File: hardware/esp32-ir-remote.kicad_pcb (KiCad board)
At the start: 2 copper layers, 80 x 55 mm, 76 parts, among them J2 USB_C_Receptacle_USB2.0_14P, J3 Qwiic_I2C, J4 GPIO_PWR, J5 EXT_IR, J6 JTAG, Q1 Q_NPN_BCE, Q2 Q_NPN_BCE, Q3 IRLML6344, Q4 2N7002, Q5 2N7002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

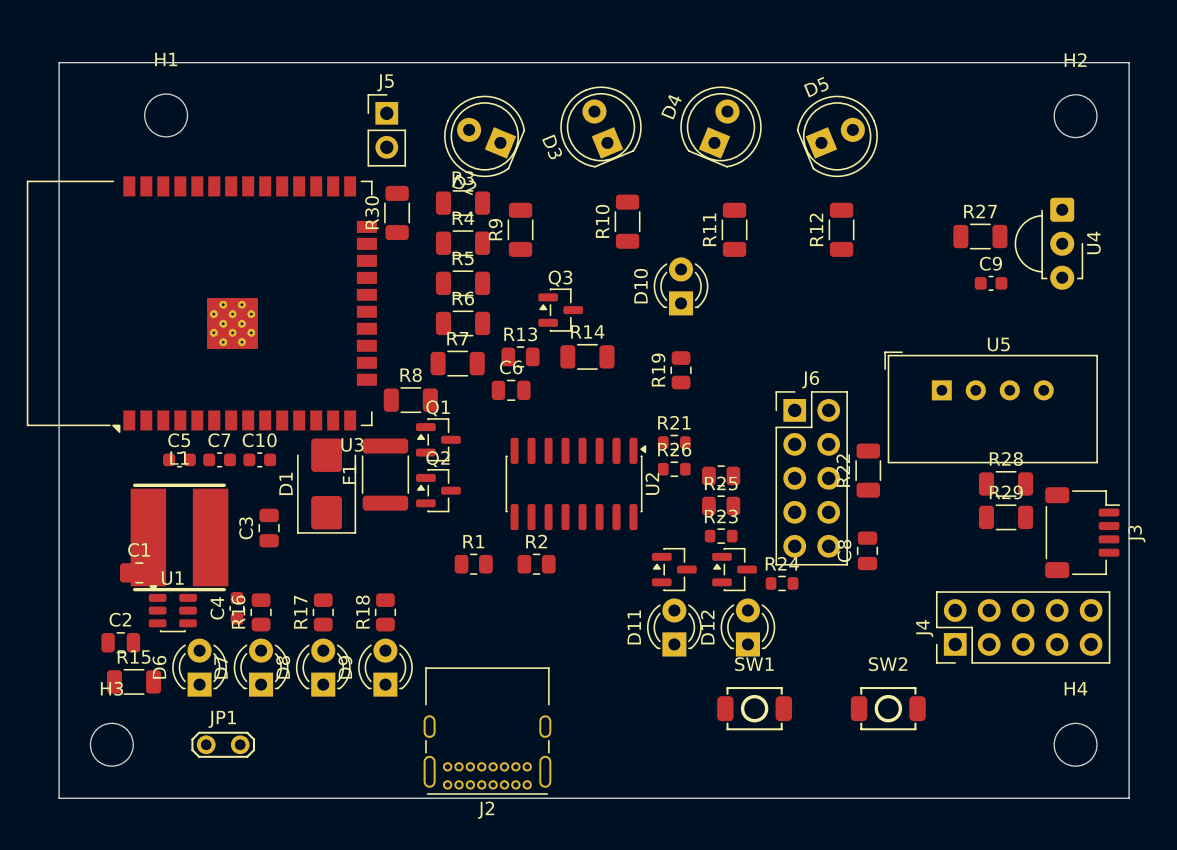
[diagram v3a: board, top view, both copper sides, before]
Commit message: H2.3 WIP: routed board v11 (1010 tracks, 143 vias, 17 legs open) + routing toolchain
- scripts/pcb_router.py: deterministic A* grid router (0.1mm grid, netclass
  widths, antenna keepout, J2 seed stubs, power-prefers-B, corridor penalties)
- scripts/pcb_finish.py: connectivity finisher with bounded rip-up + history
- scripts/pcb_pour.py: GND pours both layers + antenna keepout rule areas +
  stitching vias (not yet run)
- scripts/pcb_silk.py, scripts/drc_summary.py: silk + DRC passes (pending)
- placement deltas during routing: H1 into antenna-wedge corner (nylon screw
  note), J5/R30 west, C6 beside U2, R5-R7 pullups to NE, board min
  clearance/track relaxed to JLCPCB floor 0.127
- scripts/build-site.sh: PCB renders + GLB + interactive 3D viewer page
- hardware/bring-up.md: power-on test procedure (H3.3)
- USB-C dual-orientation D+/D- cross resolved via per-layer THT stubs
Remaining 17 unrouted legs concentrated in the EN/auto-reset cluster - being
finished by pcb_finish.py + hand-routing; DRC pass follows.
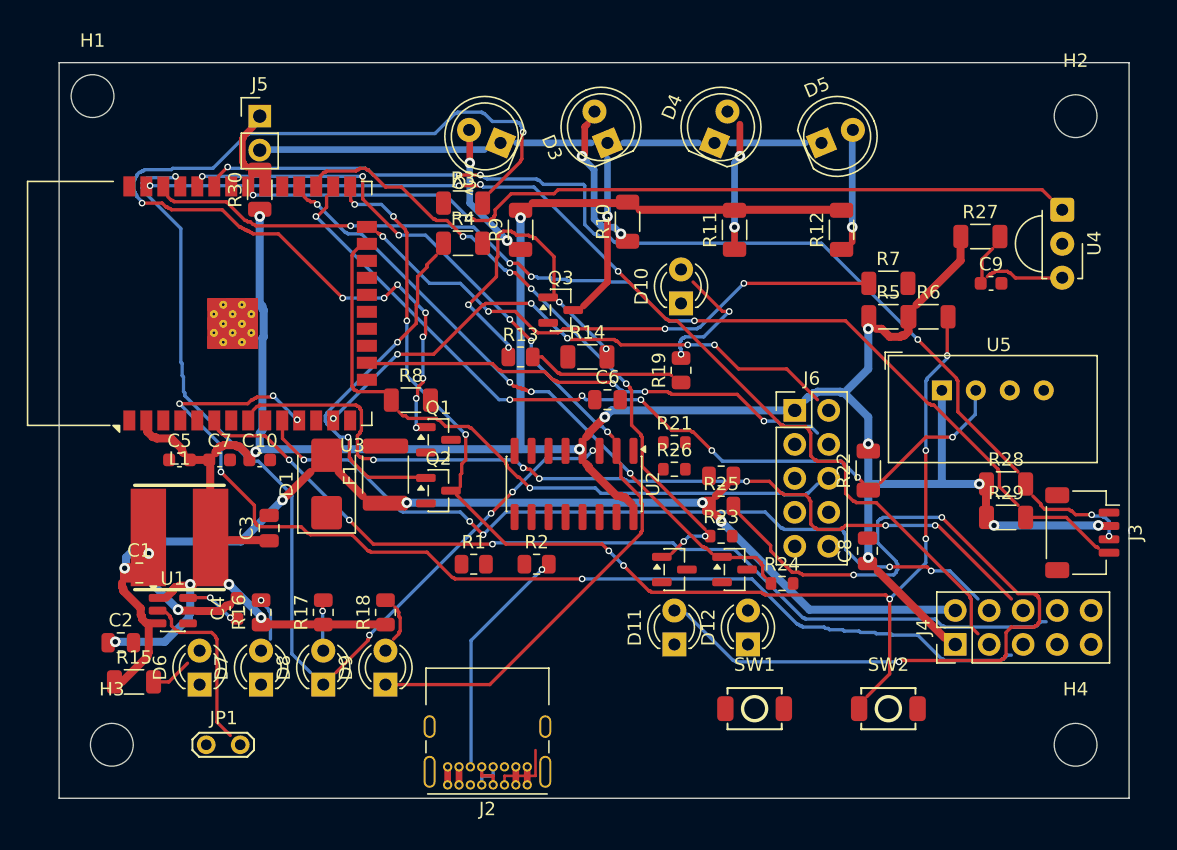
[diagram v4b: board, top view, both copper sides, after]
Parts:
- moved R6 34.8 mm to (165.0, 79.0)
- moved R7 32.8 mm to (162.0, 76.5)
- moved R5 31.9 mm to (162.0, 79.0)
- moved R30 10.4 mm to (115.0, 69.5)
- moved J5 9.50 mm to (115.0, 64.0)
- moved C6 7.23 mm to (141.0, 85.2)
- moved H1 5.69 mm to (102.5, 62.5)
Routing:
- net +3.3V: track 0.00 -> 191.0 mm, vias 0 -> 15
- net ESP_GPIO0: track 0.00 -> 92.2 mm, vias 0 -> 10
- net ESP_GPIO26: track 0.00 -> 82.0 mm, vias 0 -> 5
- net ESP_GPIO21: track 0.00 -> 80.3 mm, vias 0 -> 6
- net ESP_GPIO22: track 0.00 -> 79.7 mm, vias 0 -> 4
- net ESP_GPIO23: track 0.00 -> 79.4 mm, vias 0 -> 4
- net Net-(Q1-B): track 0.00 -> 74.0 mm, vias 0 -> 10
- net +5V: track 0.00 -> 72.0 mm, vias 0 -> 5
- net UART_TX: track 0.00 -> 71.4 mm, vias 0 -> 5
- net UART_RX: track 0.00 -> 69.3 mm, vias 0 -> 6
- net ESP_GPIO34: track 0.00 -> 68.2 mm, vias 0 -> 3
- net ESP_GPIO32: track 0.00 -> 66.6 mm, vias 0 -> 6
- net Net-(D11-A): track 0.00 -> 65.1 mm, vias 0 -> 3
- net IR_RX: track 0.00 -> 61.9 mm, vias 0 -> 2
- net TEMP_DATA: track 0.00 -> 61.6 mm, vias 0 -> 7
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
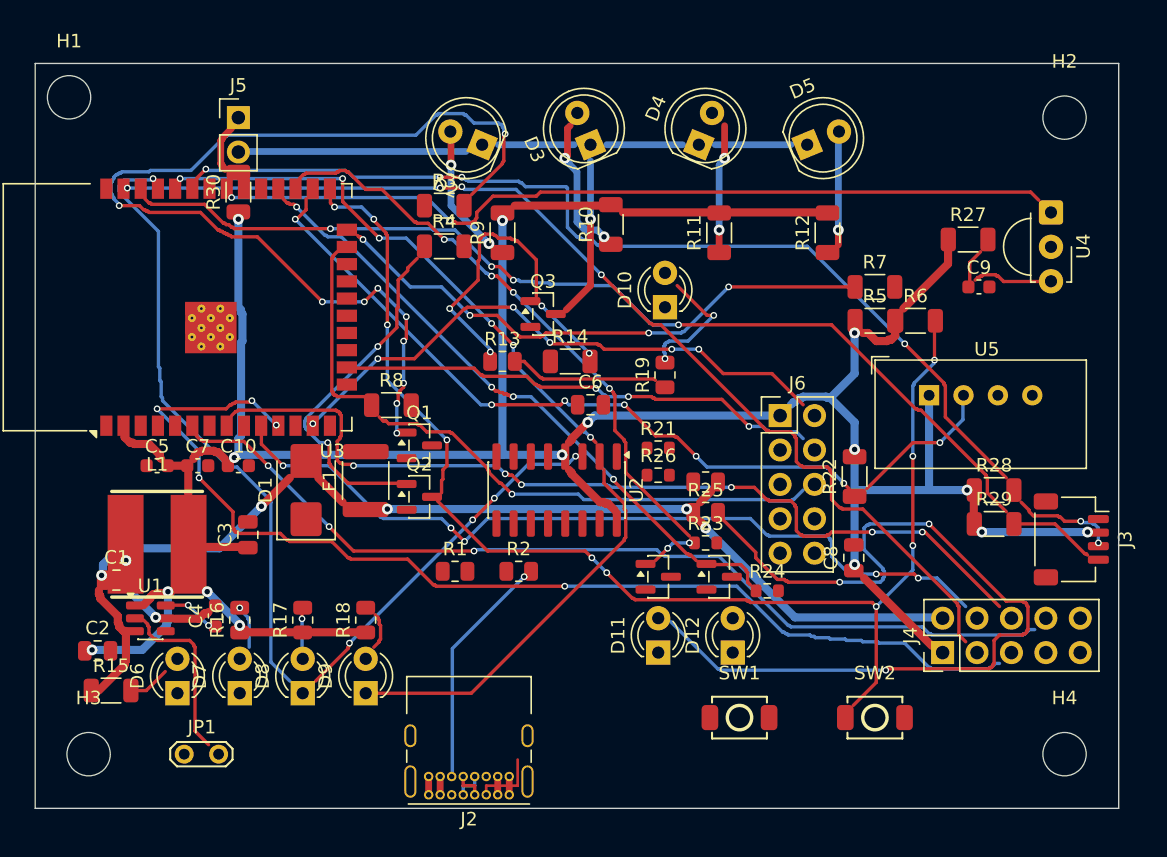
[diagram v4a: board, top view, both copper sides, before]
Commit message: H2.3: routing COMPLETE - all nets connected
Final sequence: local-families-first ordering, transit highways rerouted
around the module pad row, R5/R6/R7 pullup pitch fix (the entire ESP_EN
failure traced to R5/R6 courtyard overlap entombing R5's pad), R23
relocated to free space, connectivity finisher converged round 2:
ALL NETS CONNECTED (machine-verified component analysis of pads+tracks+vias).
Courtyards: 1 accepted exception (H1 in the antenna-wedge corner, nylon
screw documented in bring-up.md).
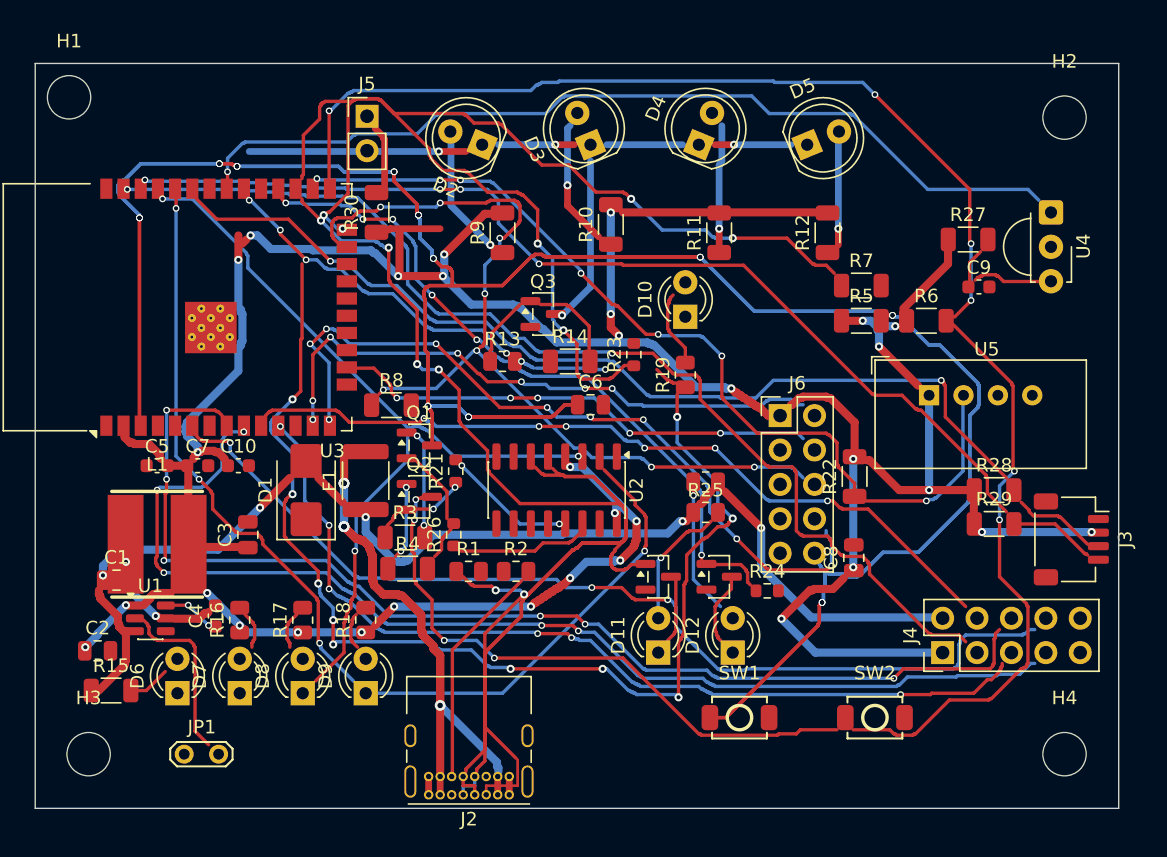
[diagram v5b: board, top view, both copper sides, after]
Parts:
- moved R3 24.7 mm to (127.3, 95.0)
- moved R4 24.0 mm to (127.5, 97.3)
- moved R26 15.7 mm to (130.9, 94.8), turned to 90 degrees
- moved R21 15.0 mm to (131.1, 90.1), turned to 90 degrees
- moved R23 14.9 mm to (144.2, 81.5), turned to 90 degrees
- moved R30 10.3 mm to (125.2, 71.0)
- moved J5 9.50 mm to (124.5, 63.9)
- moved D10 1.66 mm to (148.0, 78.7)
- moved R19 1.50 mm to (148.0, 83.0)
- moved R7 1.00 mm to (161.0, 76.4)
- moved R1 1.00 mm to (132.0, 97.5)
- moved R5 1.00 mm to (161.0, 79.0)
- moved R6 0.80 mm to (165.8, 79.0)
- moved R2 0.20 mm to (135.5, 97.5)
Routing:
- net ESP_EN: track 0.00 -> 311.4 mm, vias 0 -> 22
- net IR_TX: track 10.5 -> 117.0 mm, vias 0 -> 16
- net ESP_GPIO33: track 0.00 -> 84.3 mm, vias 0 -> 5
- net Net-(Q1-B): track 74.0 -> 6.81 mm, vias 10 -> 2
- net ESP_GPIO0: track 92.2 -> 154.2 mm
- net Net-(D11-A): track 65.1 -> 8.50 mm, vias 3 -> 1
- net ESP_GPIO12: track 0.00 -> 56.5 mm, vias 0 -> 9
- net Net-(F1-Pad2): track 2.70 -> 58.6 mm, vias 0 -> 5
- net USER_LED1: track 46.2 -> 90.0 mm
- net +3.3V: track 191.0 -> 230.8 mm, vias 15 -> 32
- net USB_D-: track 2.20 -> 36.0 mm
- net USB_D+: track 2.20 -> 34.9 mm
- net Net-(Q2-B): track 25.3 -> 5.43 mm
- net Net-(J2-CC1): track 4.92 -> 24.2 mm, vias 0 -> 2
- net ESP_GPIO15: track 47.4 -> 65.2 mm, vias 1 -> 8
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
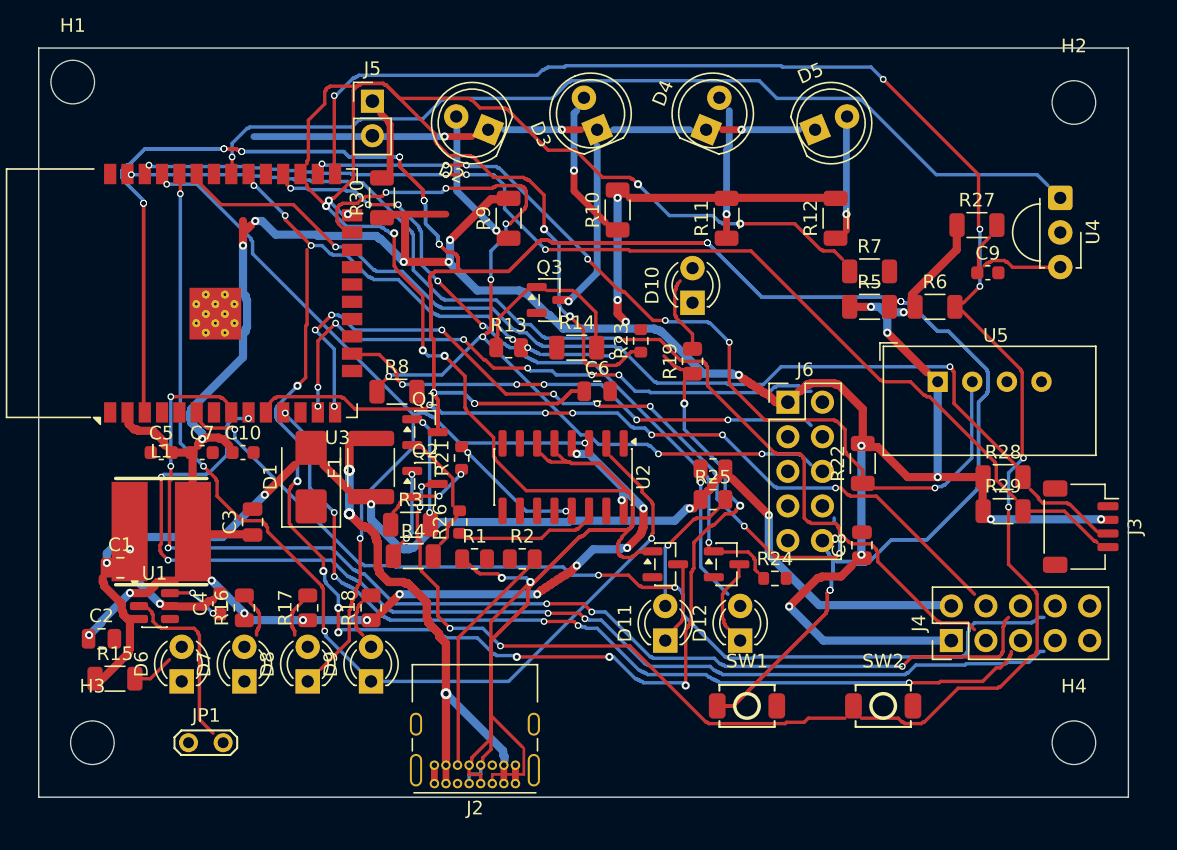
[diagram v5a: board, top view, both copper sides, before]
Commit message: H2.3/H2.4 WIP: surgical short elimination - DRC errors 150->22
Reset to routing-complete baseline, then: endpoint landings (router lands on
pad bbox cells; roundrect corners aren't copper - 68 landing segments),
SW-corner replacement (C1 pad physically overlapped L1's 2.65x7.3mm pad),
R22 clear of U5, minimal rip-cover of all shorted net pairs (the old
finisher healed same-round nets along identical paths - USB pair etc),
short-safe router-only reroute. Shorts 59->7, crossings 32->0.
6 unrouted legs + small fix families remain; pour deferred until copper
stable. Netclass clearances aligned to 0.127 fab floor; min hole 0.2.
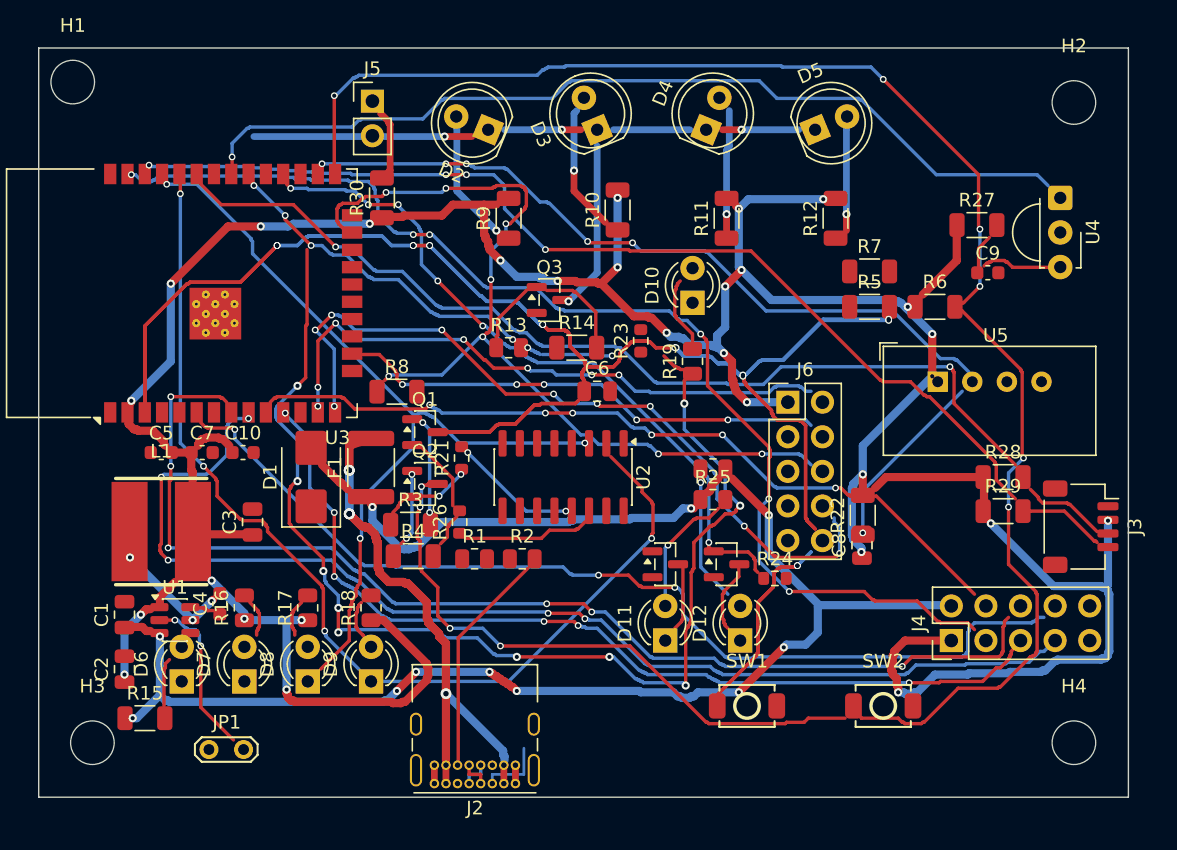
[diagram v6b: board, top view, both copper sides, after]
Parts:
- moved R22 3.80 mm to (160.5, 94.3)
- moved R15 3.64 mm to (107.8, 109.2)
- moved C1 3.46 mm to (106.3, 101.6), turned to 90 degrees
- moved C2 2.80 mm to (106.3, 105.6), turned to 90 degrees
- moved U1 1.82 mm to (110.0, 102.0)
- moved JP1 1.58 mm to (112.5, 111.5)
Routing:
- net USER_LED1: track 90.0 -> 0.00 mm, vias 6 -> 0
- net ESP_EN: track 311.4 -> 223.5 mm, vias 22 -> 16
- net ESP_GPIO2: track 52.2 -> 0.00 mm, vias 4 -> 0
- net +5V: track 77.7 -> 114.4 mm, vias 5 -> 11
- net USB_D-: track 36.0 -> 2.20 mm
- net USB_D+: track 34.9 -> 2.20 mm
- net Net-(J2-CC1): track 24.2 -> 4.92 mm, vias 2 -> 0
- net ESP_GPIO23: track 81.5 -> 85.0 mm, vias 2 -> 6
- net ESP_GPIO0: track 154.2 -> 157.2 mm
- net Net-(U1-BST): track 3.12 -> 1.08 mm, vias 2 -> 0
- net TEMP_DATA: track 65.3 -> 67.3 mm, vias 7 -> 6
- net ESP_GPIO22: track 81.3 -> 83.2 mm
- net Net-(F1-Pad2): track 58.6 -> 60.2 mm
- net +3.3V: track 230.8 -> 232.4 mm, vias 32 -> 29
- net ESP_GPIO33: track 84.3 -> 85.9 mm
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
